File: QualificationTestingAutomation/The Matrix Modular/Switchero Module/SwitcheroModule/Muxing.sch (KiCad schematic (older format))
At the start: 8 parts, among them U6 MAX14752, U7 DG408LE, U8 DS18B20_, U9 DS18B20_

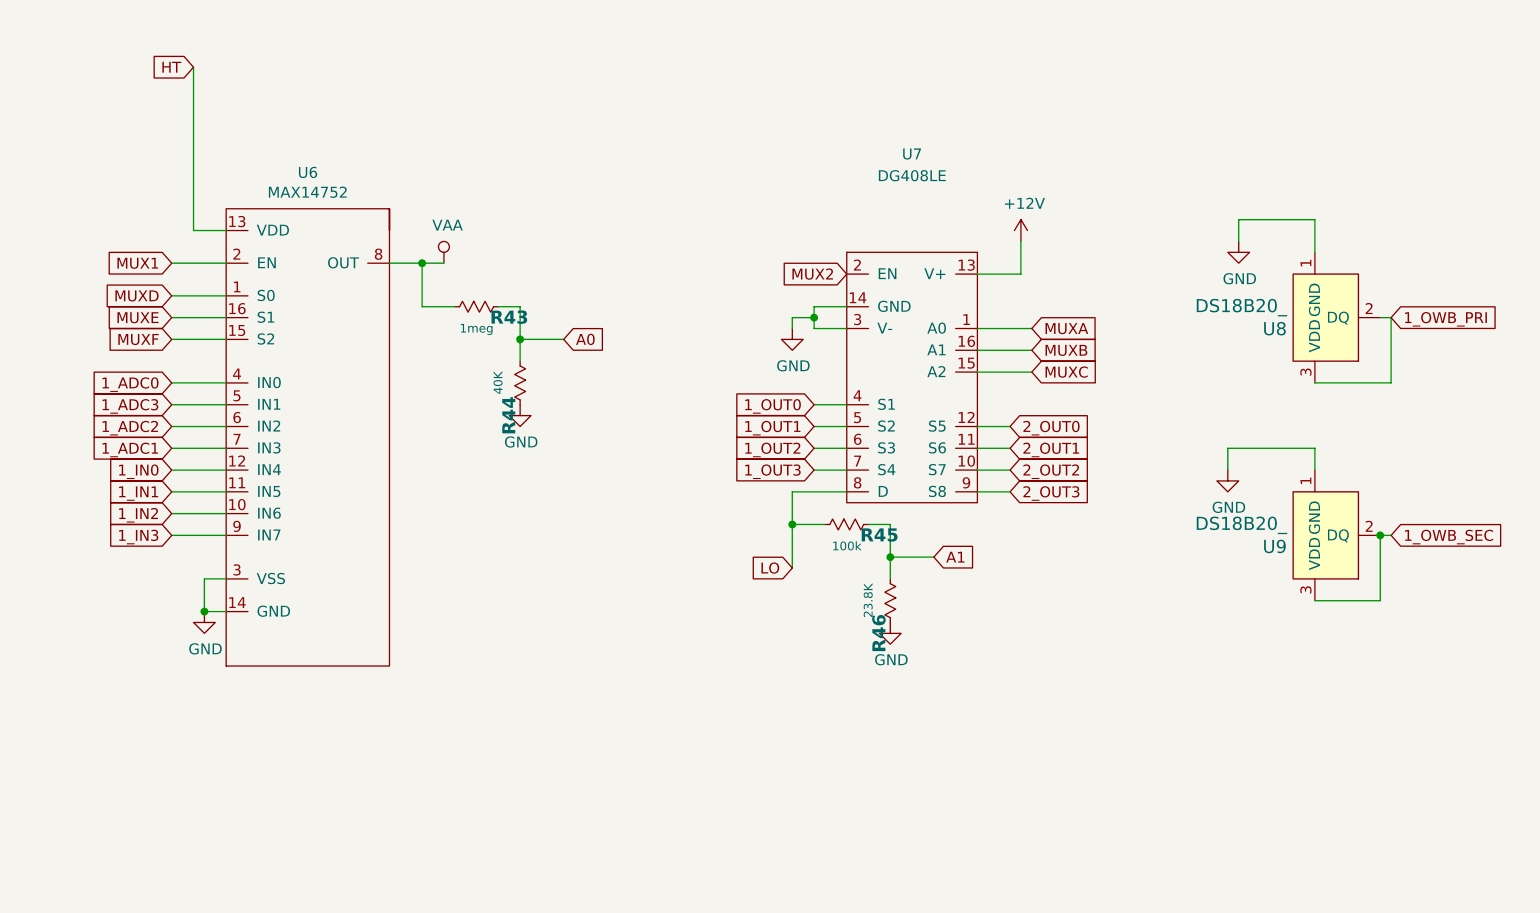
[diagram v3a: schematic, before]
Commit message: IO clean up added the 1v25 reference to Matrix Changed Some of the labels to more legible names.
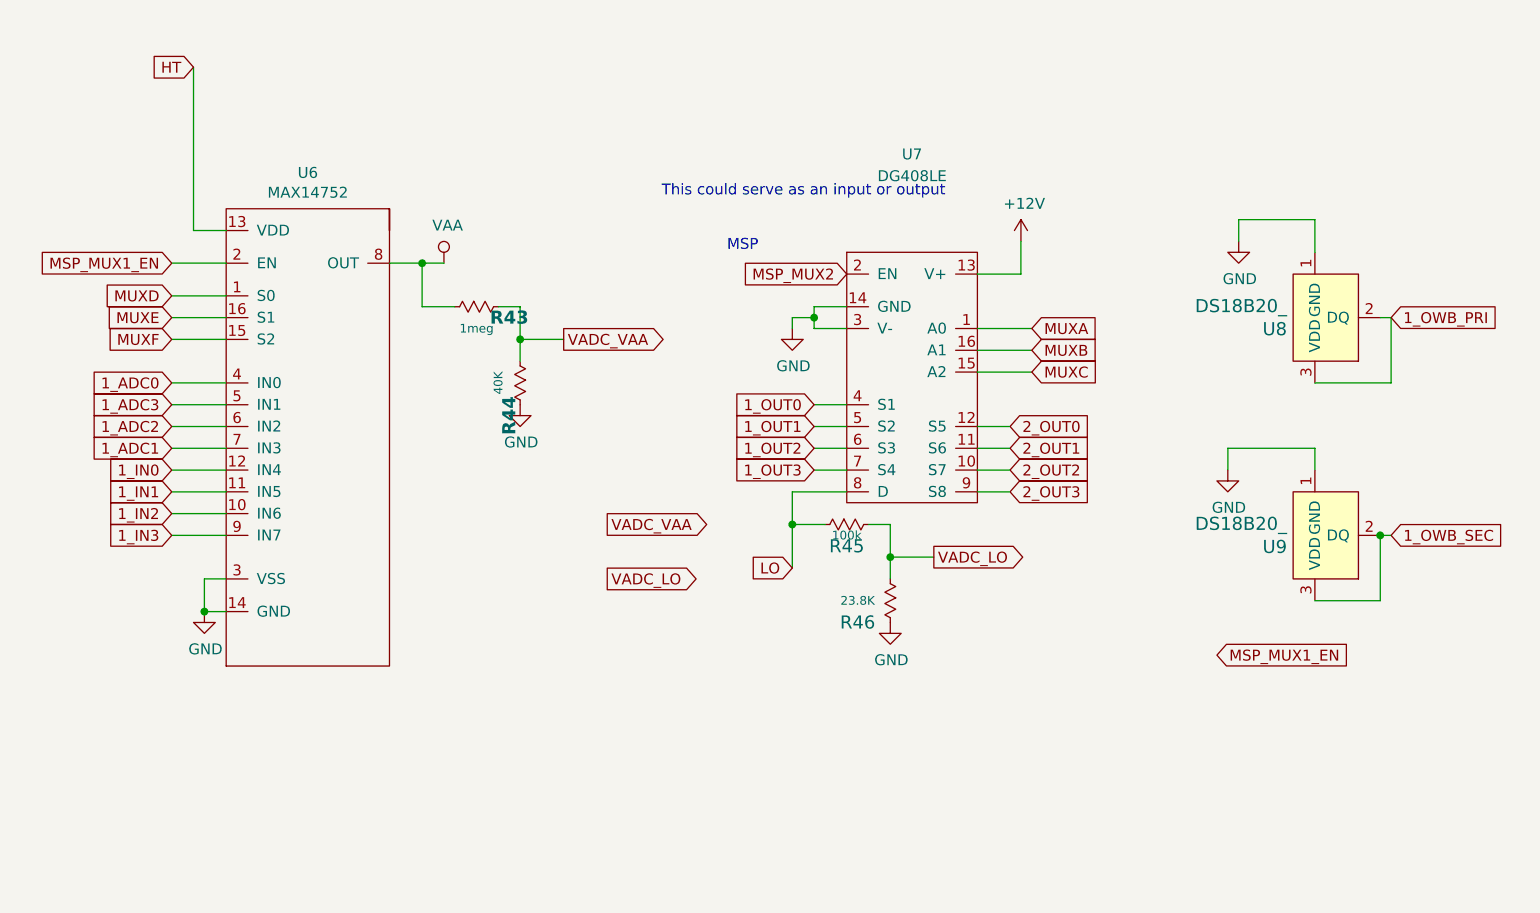
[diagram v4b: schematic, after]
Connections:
- net A0 renamed VADC_VAA
- net A1 renamed VADC_LO
- net MUX1 renamed MSP_MUX1_EN
- net MUX2 renamed MSP_MUX2
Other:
- note added: "MSP"
- note added: "This could serve as an input or output"
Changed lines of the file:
@@
 	1750 2250 1500 2250
 Text GLabel 1500 2000 0    50   Input ~ 0
-MUX1
+MSP_MUX1_EN
 Wire Wire Line
 	1500 2000 1750 2000
@@
 	1    0    0    -1
 $EndComp
-Text GLabel 4600 2050 0    50   Input ~ 0
-MUX2
 Text GLabel 5450 2300 2    50   Input ~ 0
 MUXA
@@
 Wire Wire Line
 	6750 2850 6350 2850
-Text GLabel 3300 2350 2    50   Input ~ 0
-A0
-Text GLabel 5000 3350 2    50   Input ~ 0
-A1
+Text GLabel 3300 2350 2    50   Output ~ 0
+VADC_VAA
 Wire Wire Line
 	2800 2200 2650 2200
@@
 AR Path="/5C8DF46C/5C9E4A38" Ref="R?"  Part="1"
 AR Path="/5C8DF47A/5C9E4A38" Ref="R46"  Part="1"
-F 0 "R46" H 4950 3500 60  0000 C CNB
-F 1 "23.8K" H 4800 3450 40  0000 C CNN
+F 0 "R46" V 4900 3400 60  0000 C CNN
+F 1 "23.8K" V 4800 3400 40  0000 C CNN
 F 2 "Resistor_SMD:R_0402_1005Metric" H 4800 3410 40  0001 C CNN
 F 3 "" H 4800 3650 60  0000 C CNN
@@
 AR Path="/5C8DF46C/5C9E694F" Ref="R?"  Part="1"
 AR Path="/5C8DF47A/5C9E694F" Ref="R45"  Part="1"
-F 0 "R45" H 4750 3150 60  0000 C CNB
-F 1 "100k" H 4600 3100 40  0000 C CNN
+F 0 "R45" H 4600 3100 60  0000 C CNN
+F 1 "100k" H 4600 3150 40  0000 C CNN
 F 2 "Resistor_SMD:R_0402_1005Metric" H 4600 3060 40  0001 C CNN
 F 3 "" H 4600 3300 60  0000 C CNN
@@
 	1    0    0    -1
 $EndComp
+Text Notes 3750 1700 0    50   ~ 0
+This could serve as an input or output
+Text Notes 4050 1950 0    50   ~ 0
+MSP
+Text GLabel 4600 2050 0    50   Input ~ 0
+MSP_MUX2
+Text GLabel 6300 3800 2    50   Input ~ 0
+MSP_MUX1_EN
+Text GLabel 5000 3350 2    50   Output ~ 0
+VADC_LO
+Text GLabel 3500 3200 2    50   Output ~ 0
+VADC_VAA
+Text GLabel 3500 3450 2    50   Output ~ 0
+VADC_LO
 $EndSCHEMATC

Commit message: Reefero Module PCB design
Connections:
- net MSP_MUX2 renamed MSP_MUX2_EN
- net MUXA renamed MSP_MUXA
- net MUXB renamed MSP_MUXB
- net MUXC renamed MSP_MUXC
- net MUXD renamed MSP_MUXD
- net MUXE renamed MSP_MUXE
- net MUXF renamed MSP_MUXF
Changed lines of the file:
@@
 Wire Wire Line
 	1650 3450 1650 3600
-Text GLabel 1500 2350 0    50   Input ~ 0
-MUXF
-Text GLabel 1500 2150 0    50   Input ~ 0
-MUXD
-Text GLabel 1500 2250 0    50   Input ~ 0
-MUXE
 Wire Wire Line
 	1500 2350 1750 2350
@@
 	1    0    0    -1
 $EndComp
-Text GLabel 5450 2300 2    50   Input ~ 0
-MUXA
-Text GLabel 5450 2400 2    50   Input ~ 0
-MUXB
-Text GLabel 5450 2500 2    50   Input ~ 0
-MUXC
-Wire Wire Line
-	5450 2300 5200 2300
-Wire Wire Line
-	5200 2400 5450 2400
-Wire Wire Line
-	5200 2500 5450 2500
 Wire Wire Line
 	4350 3050 4600 3050
@@
 Text GLabel 4350 3400 0    50   Input ~ 0
 LO
-Text GLabel 1600 1100 0    50   Input ~ 0
+Text GLabel 1600 1100 1    50   Input ~ 0
 HT
 Wire Wire Line
@@
 Text Notes 3750 1700 0    50   ~ 0
 This could serve as an input or output
-Text Notes 4050 1950 0    50   ~ 0
+Text Notes 3950 1950 0    50   ~ 0
 MSP
-Text GLabel 4600 2050 0    50   Input ~ 0
-MSP_MUX2
-Text GLabel 6300 3800 2    50   Input ~ 0
-MSP_MUX1_EN
+Text GLabel 4500 2050 0    50   Input ~ 0
+MSP_MUX2_EN
 Text GLabel 5000 3350 2    50   Output ~ 0
 VADC_LO
-Text GLabel 3500 3200 2    50   Output ~ 0
-VADC_VAA
-Text GLabel 3500 3450 2    50   Output ~ 0
-VADC_LO
+Text GLabel 5350 2300 2    50   Input ~ 0
+MSP_MUXA
+Text GLabel 5350 2400 2    50   Input ~ 0
+MSP_MUXB
+Text GLabel 5350 2500 2    50   Input ~ 0
+MSP_MUXC
+Text GLabel 1500 2350 0    50   Input ~ 0
+MSP_MUXF
+Text GLabel 1500 2150 0    50   Input ~ 0
+MSP_MUXD
+Text GLabel 1500 2250 0    50   Input ~ 0
+MSP_MUXE
+Wire Wire Line
+	4600 2050 4500 2050
+Wire Wire Line
+	5350 2500 5200 2500
+Wire Wire Line
+	5200 2400 5350 2400
+Wire Wire Line
+	5350 2300 5200 2300
 $EndSCHEMATC
